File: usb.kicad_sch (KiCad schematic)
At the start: 134 parts, among them J3 USB4105-GF-A, J4 WE_632723300011_alt_symbol, Q1 NX138BKMYL, Q2 NX138BKMYL, Q3 NX138BKMYL, U10 TUSB1046-DCI, U11 TPD4E05U06QDQARQ1, U12 AP22615, U13 TPD4E05U06QDQARQ1, U14 TPD4E05U06QDQARQ1, U15 TPD4E05U06QDQARQ1, U16 TPD4E05U06QDQARQ1, U5 FT230XQ-R, U6 TPS65988, U7 W25Q80DVUXIE_TR, U8 TPS7B8133DRVR, U9 AP22615

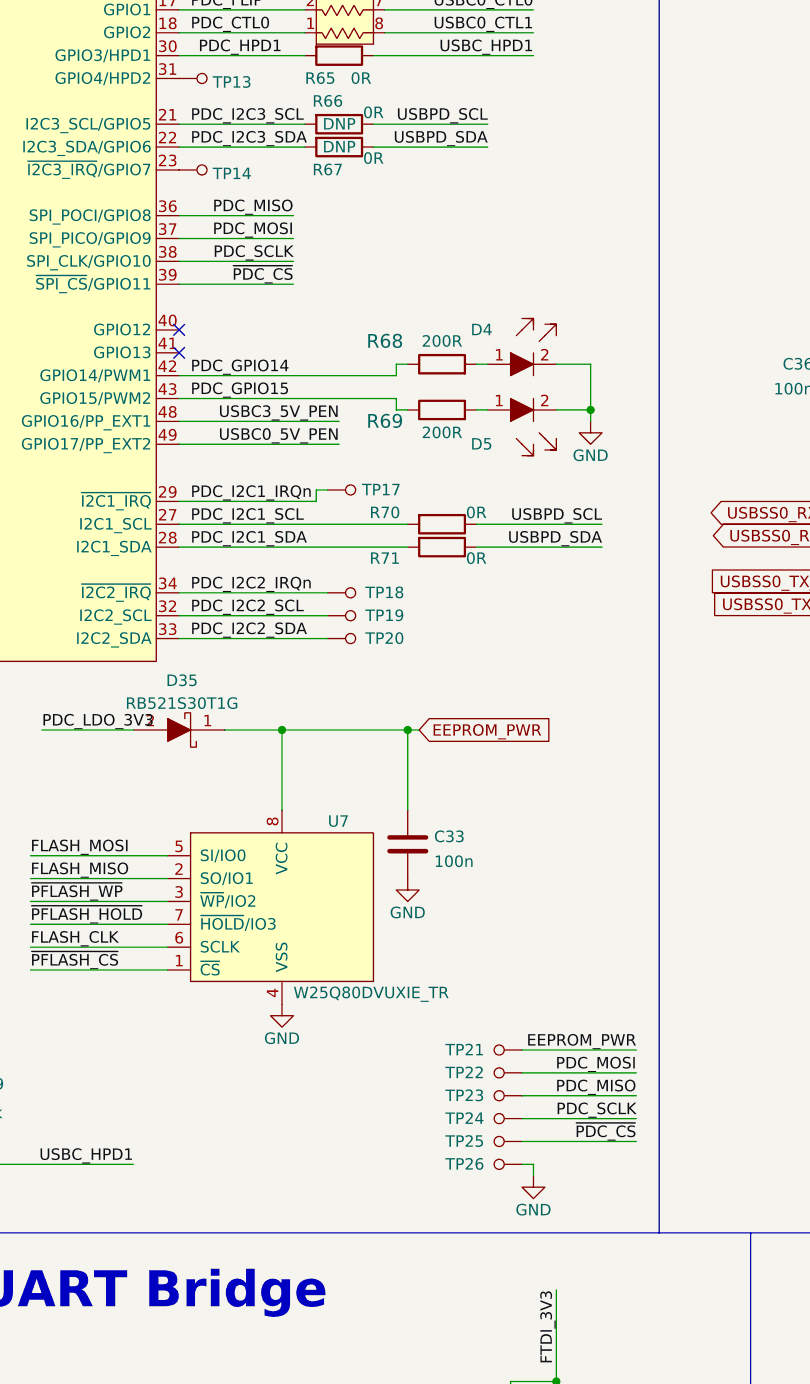
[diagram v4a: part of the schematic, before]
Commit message: Routed more low speed signal and power
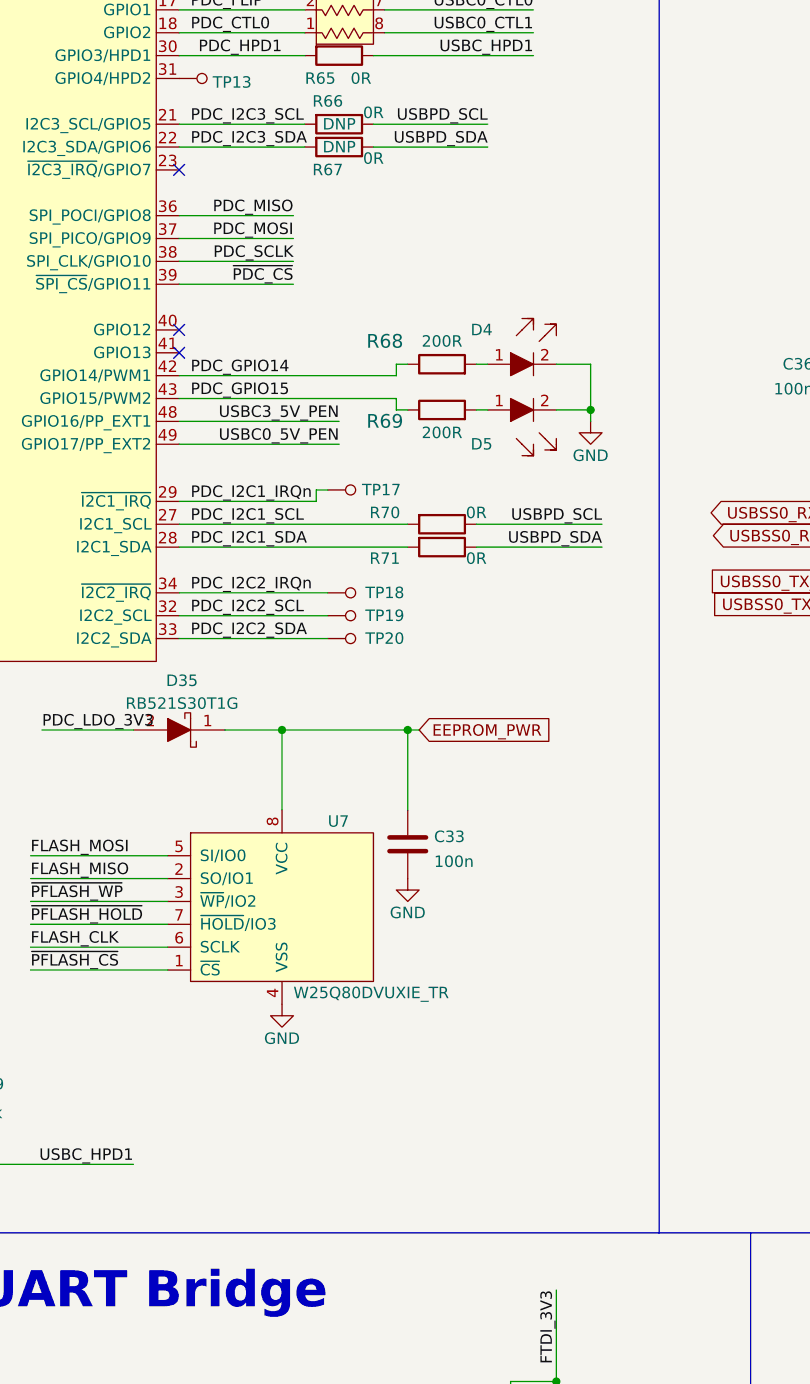
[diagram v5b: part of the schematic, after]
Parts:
- removed TP14, TP21, TP22, TP23, TP24, TP25, TP26: TP_SMD_0_75MM, antmicro-footprints:Testpoint_smd_0_75mm, symbol antmicroTestPoints:TP_SMD_0_75MM
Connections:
- no-connect marks 17 -> 18
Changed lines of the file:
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@@
   (no_connect (at 265.43 262.89))
   (no_connect (at 90.17 215.9))
+  (no_connect (at 92.71 63.5))
   (no_connect (at 292.1 135.89))
   (no_connect (at 294.64 135.89))
@@
     (stroke (width 0) (type solid) (color 0 0 0 0))
   )
-  (wire (pts (xy 143.51 168.91) (xy 130.81 168.91))
-    (stroke (width 0) (type default) (color 0 0 0 0))
-  )
   (wire (pts (xy 255.27 63.5) (xy 255.27 64.77))
     (stroke (width 0) (type default) (color 0 0 0 0))
@@
     (stroke (width 0) (type default) (color 0 0 0 0))
   )
-  (wire (pts (xy 130.81 173.99) (xy 132.08 173.99))
-    (stroke (width 0) (type default) (color 0 0 0 0))
-  )
   (wire (pts (xy 261.62 48.26) (xy 275.59 48.26))
     (stroke (width 0) (type default) (color 0 0 0 0))
@@
     (stroke (width 0) (type default) (color 0 0 0 0))
   )
-  (wire (pts (xy 143.51 171.45) (xy 130.81 171.45))
-    (stroke (width 0) (type default) (color 0 0 0 0))
-  )
   (wire (pts (xy 220.98 218.44) (xy 220.98 219.71))
     (stroke (width 0) (type default) (color 0 0 0 0))
@@
     (stroke (width 0) (type default) (color 0 0 0 0))
   )
-  (wire (pts (xy 132.08 173.99) (xy 132.08 175.26))
-    (stroke (width 0) (type default) (color 0 0 0 0))
-  )
   (wire (pts (xy 295.91 58.42) (xy 295.91 59.69))
     (stroke (width 0) (type default) (color 0 0 0 0))
@@
     (stroke (width 0) (type solid) (color 0 0 0 0))
   )
-  (wire (pts (xy 143.51 163.83) (xy 130.81 163.83))
-    (stroke (width 0) (type default) (color 0 0 0 0))
-  )
   (wire (pts (xy 361.95 64.77) (xy 361.95 78.74))
     (stroke (width 0) (type default) (color 0 0 0 0))
@@
     (stroke (width 0) (type default) (color 0 0 0 0))
   )
-  (wire (pts (xy 130.81 161.29) (xy 143.51 161.29))
-    (stroke (width 0) (type default) (color 0 0 0 0))
-  )
   (wire (pts (xy 238.76 255.27) (xy 245.11 255.27))
     (stroke (width 0) (type default) (color 0 0 0 0))
@@
     (stroke (width 0) (type default) (color 0 0 0 0))
   )
-  (wire (pts (xy 143.51 166.37) (xy 130.81 166.37))
-    (stroke (width 0) (type default) (color 0 0 0 0))
-  )
   (wire (pts (xy 236.22 124.46) (xy 273.05 124.46))
     (stroke (width 0) (type default) (color 0 0 0 0))
@@
     (effects (font (size 1.27 1.27)) (justify left bottom))
   )
-  (label "PDC_MOSI" (at 143.51 163.83 180)
-    (effects (font (size 1.27 1.27)) (justify right bottom))
-  )
   (label "USBC0_RX1_P" (at 238.76 101.6 0)
     (effects (font (size 1.27 1.27)) (justify left bottom))
@@
     (effects (font (size 1.27 1.27)) (justify left bottom))
   )
-  (label "~{PDC_CS}" (at 143.51 171.45 180)
-    (effects (font (size 1.27 1.27)) (justify right bottom))
-  )
   (label "USBC0_EQ1" (at 237.49 162.56 0)
     (effects (font (size 1.27 1.27)) (justify left bottom))
@@
     (effects (font (size 1.27 1.27)) (justify left bottom))
   )
-  (label "PDC_SCLK" (at 143.51 168.91 180)
-    (effects (font (size 1.27 1.27)) (justify right bottom))
-  )
   (label "FLASH_MOSI" (at 76.2 139.7 0)
     (effects (font (size 1.27 1.27)) (justify left bottom))
@@
     (effects (font (size 1.27 1.27)) (justify left bottom))
   )
-  (label "EEPROM_PWR" (at 143.51 161.29 180)
-    (effects (font (size 1.27 1.27)) (justify right bottom))
-  )
   (label "FTDI_LED_RX" (at 148.59 219.71 180)
     (effects (font (size 1.27 1.27)) (justify right bottom))
@@
     (effects (font (size 1.27 1.27)) (justify left bottom))
   )
-  (label "PDC_MISO" (at 143.51 166.37 180)
-    (effects (font (size 1.27 1.27)) (justify right bottom))
-  )
   (label "FTDI_LED_RX" (at 93.98 222.25 180)
     (effects (font (size 1.27 1.27)) (justify right bottom))
@@
     (pin "1")
   )
-  (symbol (lib_id "antmicroTestPoints:TP_SMD_0_75MM") (at 128.27 171.45 270) (unit 1)
-    (in_bom yes) (on_board yes)
-    (property "Reference" "TP25" (id 0) (at 124.46 171.45 90))
-    (property "Value" "TP_SMD_0_75MM" (id 1) (at 125.73 171.45 0)
-      (effects (font (size 1.27 1.27)) hide)
-    )
-    (property "Footprint" "antmicro-footprints:Testpoint_smd_0_75mm" (id 2) (at 133.35 176.53 0)
-      (effects (font (size 1.524 1.524)) (justify left) hide)
-    )
-    (property "Datasheet" "" (id 3) (at 135.89 176.53 0)
-      (effects (font (size 1.524 1.524)) (justify left) hide)
-    )
-    (pin "1")
-  )
   (symbol (lib_id "antmicroTVSDiodes:TPD4E05U06QDQARQ1") (at 318.77 137.16 270) (unit 1)
     (in_bom yes) (on_board yes) (fields_autoplaced)
@@
     (pin "3")
   )
-  (symbol (lib_id "antmicroTestPoints:TP_SMD_0_75MM") (at 128.27 168.91 270) (unit 1)
-    (in_bom yes) (on_board yes)
-    (property "Reference" "TP24" (id 0) (at 124.46 168.91 90))
-    (property "Value" "TP_SMD_0_75MM" (id 1) (at 125.73 168.91 0)
-      (effects (font (size 1.27 1.27)) hide)
-    )
-    (property "Footprint" "antmicro-footprints:Testpoint_smd_0_75mm" (id 2) (at 133.35 173.99 0)
-      (effects (font (size 1.524 1.524)) (justify left) hide)
-    )
-    (property "Datasheet" "" (id 3) (at 135.89 173.99 0)
-      (effects (font (size 1.524 1.524)) (justify left) hide)
-    )
-    (pin "1")
-  )
   (symbol (lib_id "antmicroResistors0402:R_0R_0402") (at 242.57 74.93 90) (unit 1)
     (in_bom no) (on_board yes)
@@
     (pin "2")
   )
-  (symbol (lib_id "antmicroTestPoints:TP_SMD_0_75MM") (at 128.27 166.37 270) (unit 1)
-    (in_bom yes) (on_board yes)
-    (property "Reference" "TP23" (id 0) (at 124.46 166.37 90))
-    (property "Value" "TP_SMD_0_75MM" (id 1) (at 125.73 166.37 0)
-      (effects (font (size 1.27 1.27)) hide)
-    )
-    (property "Footprint" "antmicro-footprints:Testpoint_smd_0_75mm" (id 2) (at 133.35 171.45 0)
-      (effects (font (size 1.524 1.524)) (justify left) hide)
-    )
-    (property "Datasheet" "" (id 3) (at 135.89 171.45 0)
-      (effects (font (size 1.524 1.524)) (justify left) hide)
-    )
-    (pin "1")
-  )
   (symbol (lib_id "antmicroPMICVoltageRegulatorsLinear:TPS7B8133DRVR") (at 121.92 256.54 0) (unit 1)
     (in_bom yes) (on_board yes) (fields_autoplaced)
@@
     (pin "1")
   )
-  (symbol (lib_id "antmicroTestPoints:TP_SMD_0_75MM") (at 128.27 161.29 270) (unit 1)
-    (in_bom yes) (on_board yes)
-    (property "Reference" "TP21" (id 0) (at 124.46 161.29 90))
-    (property "Value" "TP_SMD_0_75MM" (id 1) (at 125.73 161.29 0)
-      (effects (font (size 1.27 1.27)) hide)
-    )
-    (property "Footprint" "antmicro-footprints:Testpoint_smd_0_75mm" (id 2) (at 133.35 166.37 0)
-      (effects (font (size 1.524 1.524)) (justify left) hide)
-    )
-    (property "Datasheet" "" (id 3) (at 135.89 166.37 0)
-      (effects (font (size 1.524 1.524)) (justify left) hide)
-    )
-    (pin "1")
-  )
   (symbol (lib_id "antmicroResistors0402:R_1k_0402") (at 269.24 167.64 0) (unit 1)
     (in_bom yes) (on_board yes)
@@
     (pin "2")
   )
-  (symbol (lib_id "antmicroTestPoints:TP_SMD_0_75MM") (at 128.27 173.99 270) (unit 1)
-    (in_bom yes) (on_board yes)
-    (property "Reference" "TP26" (id 0) (at 124.46 173.99 90))
-    (property "Value" "TP_SMD_0_75MM" (id 1) (at 125.73 173.99 0)
-      (effects (font (size 1.27 1.27)) hide)
-    )
-    (property "Footprint" "antmicro-footprints:Testpoint_smd_0_75mm" (id 2) (at 133.35 179.07 0)
-      (effects (font (size 1.524 1.524)) (justify left) hide)
-    )
-    (property "Datasheet" "" (id 3) (at 135.89 179.07 0)
-      (effects (font (size 1.524 1.524)) (justify left) hide)
-    )
-    (pin "1")
-  )
   (symbol (lib_id "antmicroTransistorsFETsMOSFETsSingle:NX138BKMYL") (at 58.42 173.99 270) (unit 1)
     (in_bom yes) (on_board yes)
@@
     (pin "2")
   )
-  (symbol (lib_id "antmicroTestPoints:TP_SMD_0_75MM") (at 128.27 163.83 270) (unit 1)
-    (in_bom yes) (on_board yes)
-    (property "Reference" "TP22" (id 0) (at 124.46 163.83 90))
-    (property "Value" "TP_SMD_0_75MM" (id 1) (at 125.73 163.83 0)
-      (effects (font (size 1.27 1.27)) hide)
-    )
-    (property "Footprint" "antmicro-footprints:Testpoint_smd_0_75mm" (id 2) (at 133.35 168.91 0)
-      (effects (font (size 1.524 1.524)) (justify left) hide)
-    )
-    (property "Datasheet" "" (id 3) (at 135.89 168.91 0)
-      (effects (font (size 1.524 1.524)) (justify left) hide)
-    )
-    (pin "1")
-  )
   (symbol (lib_id "power:GND") (at 332.74 137.16 0) (unit 1)
     (in_bom yes) (on_board yes) (fields_autoplaced)
@@
     (pin "2")
   )
-  (symbol (lib_id "antmicroTestPoints:TP_SMD_0_75MM") (at 95.25 63.5 90) (unit 1)
-    (in_bom yes) (on_board yes) (fields_autoplaced)
-    (property "Reference" "TP14" (id 0) (at 96.4438 63.9338 90)
-      (effects (font (size 1.27 1.27)) (justify right))
-    )
-    (property "Value" "TP_SMD_0_75MM" (id 1) (at 97.79 63.5 0)
-      (effects (font (size 1.27 1.27)) hide)
-    )
-    (property "Footprint" "antmicro-footprints:Testpoint_smd_0_75mm" (id 2) (at 90.17 58.42 0)
-      (effects (font (size 1.524 1.524)) (justify left) hide)
-    )
-    (property "Datasheet" "" (id 3) (at 87.63 58.42 0)
-      (effects (font (size 1.524 1.524)) (justify left) hide)
-    )
-    (pin "1")
-  )
   (symbol (lib_id "antmicroLEDIndicationDiscrete:LTST-C190GKT") (at 132.08 90.17 0) (mirror x) (unit 1)
     (in_bom yes) (on_board yes)
@@
     (pin "Shell")
   )
-  (symbol (lib_id "power:GND") (at 132.08 175.26 0) (unit 1)
-    (in_bom yes) (on_board yes)
-    (property "Reference" "#PWR064" (id 0) (at 132.08 181.61 0)
-      (effects (font (size 1.27 1.27)) hide)
-    )
-    (property "Value" "GND" (id 1) (at 132.08 179.07 0))
-    (property "Footprint" "" (id 2) (at 132.08 175.26 0)
-      (effects (font (size 1.27 1.27)) hide)
-    )
-    (property "Datasheet" "" (id 3) (at 132.08 175.26 0)
-      (effects (font (size 1.27 1.27)) hide)
-    )
-    (pin "1")
-  )
   (symbol (lib_id "antmicroResistors0402:R_2k2_0402") (at 220.98 213.36 90) (unit 1)

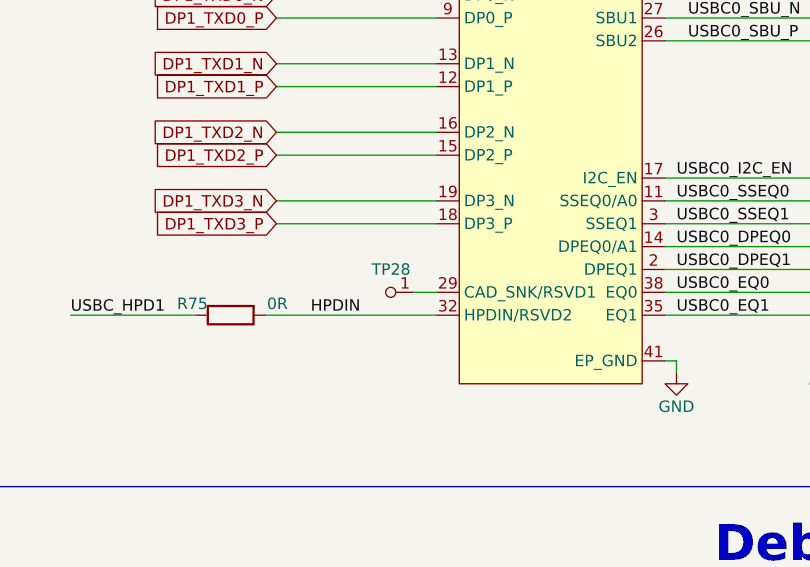
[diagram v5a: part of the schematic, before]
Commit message: Fixed DRC errors, fixed swapped SDA/SCL
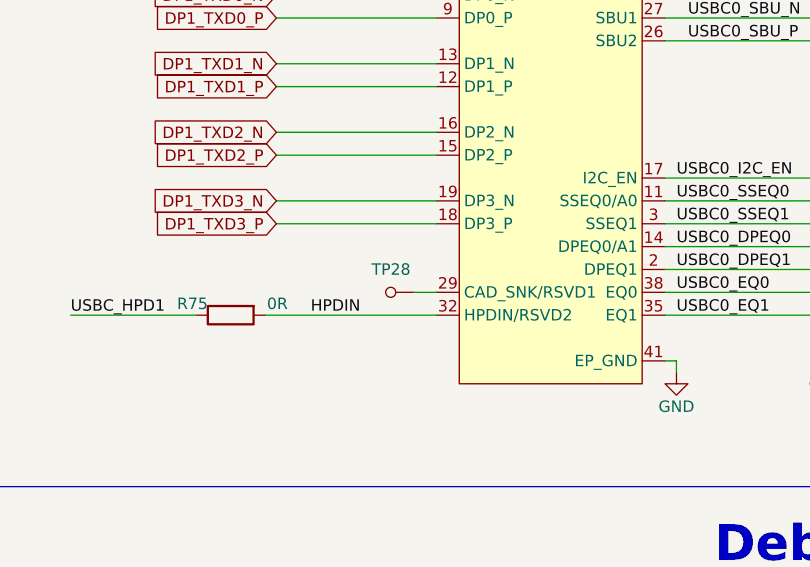
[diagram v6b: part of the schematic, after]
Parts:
- TP28: footprint antmicro-footprints:TP-R-1.5 -> antmicro-footprints:Testpoint_smd_0_75mm; symbol antmicroTestPoints:TP -> antmicroTestPoints:TP_SMD_0_75MM
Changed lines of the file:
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@@
     (pin "2")
   )
-  (symbol (lib_id "antmicroTestPoints:TP") (at 205.74 160.02 270) (unit 1)
+  (symbol (lib_id "antmicroTestPoints:TP_SMD_0_75MM") (at 205.74 160.02 270) (unit 1)
     (in_bom yes) (on_board yes) (fields_autoplaced)
     (property "Reference" "TP28" (id 0) (at 205.7781 157.48 90))
@@
       (effects (font (size 1.27 1.27)) hide)
     )
-    (property "Footprint" "antmicro-footprints:TP-R-1.5" (id 2) (at 205.74 160.02 0)
-      (effects (font (size 1.27 1.27)) hide)
+    (property "Footprint" "antmicro-footprints:Testpoint_smd_0_75mm" (id 2) (at 210.82 165.1 0)
+      (effects (font (size 1.524 1.524)) (justify left) hide)
     )
-    (property "Datasheet" "" (id 3) (at 205.74 160.02 0)
-      (effects (font (size 1.27 1.27)) hide)
+    (property "Datasheet" "" (id 3) (at 213.36 165.1 0)
+      (effects (font (size 1.524 1.524)) (justify left) hide)
     )
     (pin "1")

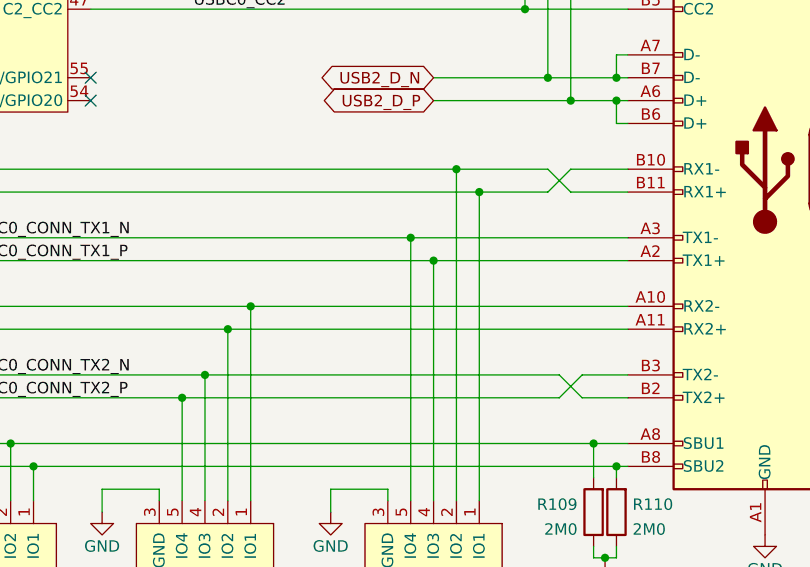
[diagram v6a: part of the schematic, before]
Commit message: Fixed swapped CSI signals
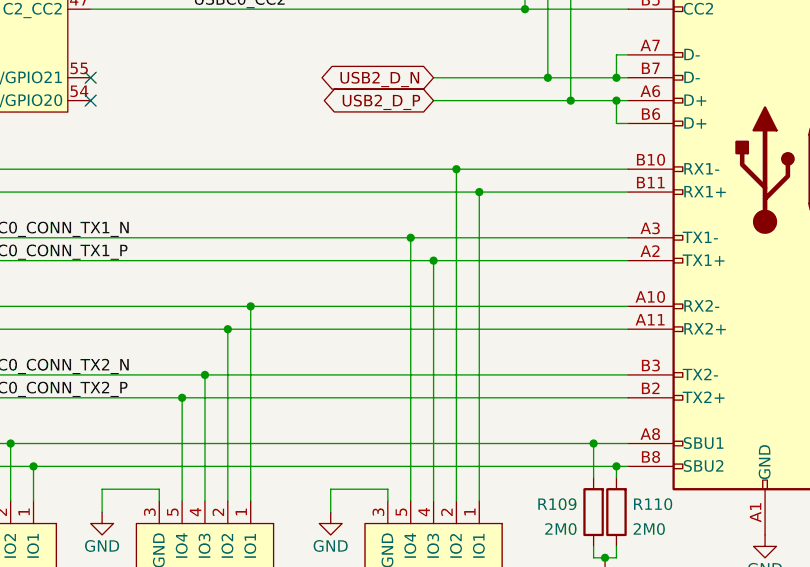
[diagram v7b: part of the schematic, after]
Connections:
- net USBC0_CONN_TX2_N: now also J4.B3 (TX2-); no longer J4.B2 (TX2+)
- net USBC0_CONN_TX2_P: now also J4.B2 (TX2+); no longer J4.B3 (TX2-)
- net USBC0_RX1_N: now also J4.B10 (RX1-); no longer J4.B11 (RX1+)
- net USBC0_RX1_P: now also J4.B11 (RX1+); no longer J4.B10 (RX1-)
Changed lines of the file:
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@@
-    (stroke (width 0) (type default) (color 0 0 0 0))
-  )
-  (wire (pts (xy 358.14 121.92) (xy 360.68 124.46))
     (stroke (width 0) (type default) (color 0 0 0 0))
   )
@@
     (stroke (width 0) (type default) (color 0 0 0 0))
   )
-  (wire (pts (xy 356.87 99.06) (xy 359.41 101.6))
-    (stroke (width 0) (type default) (color 0 0 0 0))
-  )
   (wire (pts (xy 171.45 101.6) (xy 168.91 104.14))
     (stroke (width 0) (type default) (color 0 0 0 0))
@@
   )
   (wire (pts (xy 242.57 83.82) (xy 259.08 83.82))
-    (stroke (width 0) (type default) (color 0 0 0 0))
-  )
-  (wire (pts (xy 359.41 99.06) (xy 365.76 99.06))
     (stroke (width 0) (type default) (color 0 0 0 0))
   )
@@
     (stroke (width 0) (type default) (color 0 0 0 0))
   )
-  (wire (pts (xy 360.68 121.92) (xy 365.76 121.92))
+  (wire (pts (xy 318.77 121.92) (xy 365.76 121.92))
     (stroke (width 0) (type default) (color 0 0 0 0))
   )
@@
     (stroke (width 0) (type default) (color 0 0 0 0))
   )
-  (wire (pts (xy 359.41 101.6) (xy 365.76 101.6))
-    (stroke (width 0) (type default) (color 0 0 0 0))
-  )
   (wire (pts (xy 344.17 91.44) (xy 359.41 91.44))
     (stroke (width 0) (type default) (color 0 0 0 0))
@@
     (stroke (width 0) (type default) (color 0 0 0 0))
   )
-  (wire (pts (xy 316.23 124.46) (xy 358.14 124.46))
-    (stroke (width 0) (type default) (color 0 0 0 0))
-  )
   (wire (pts (xy 273.05 139.7) (xy 276.86 139.7))
     (stroke (width 0) (type default) (color 0 0 0 0))
@@
     (stroke (width 0) (type default) (color 0 0 0 0))
   )
-  (wire (pts (xy 359.41 99.06) (xy 356.87 101.6))
-    (stroke (width 0) (type default) (color 0 0 0 0))
-  )
   (wire (pts (xy 344.17 109.22) (xy 365.76 109.22))
     (stroke (width 0) (type default) (color 0 0 0 0))
@@
     (stroke (width 0) (type default) (color 0 0 0 0))
   )
-  (wire (pts (xy 349.25 101.6) (xy 356.87 101.6))
+  (wire (pts (xy 349.25 101.6) (xy 365.76 101.6))
     (stroke (width 0) (type default) (color 0 0 0 0))
   )
@@
     (stroke (width 0) (type default) (color 0 0 0 0))
   )
-  (wire (pts (xy 346.71 99.06) (xy 356.87 99.06))
+  (wire (pts (xy 346.71 99.06) (xy 365.76 99.06))
     (stroke (width 0) (type default) (color 0 0 0 0))
   )
@@
     (stroke (width 0) (type default) (color 0 0 0 0))
   )
-  (wire (pts (xy 318.77 121.92) (xy 358.14 121.92))
-    (stroke (width 0) (type default) (color 0 0 0 0))
-  )
   (wire (pts (xy 92.71 68.58) (xy 105.41 68.58))
     (stroke (width 0) (type default) (color 0 0 0 0))
@@
     (stroke (width 0) (type default) (color 0 0 0 0))
   )
-  (wire (pts (xy 360.68 124.46) (xy 365.76 124.46))
+  (wire (pts (xy 316.23 124.46) (xy 365.76 124.46))
     (stroke (width 0) (type default) (color 0 0 0 0))
   )
@@
     (stroke (width 0) (type default) (color 0 0 0 0))
   )
-  (wire (pts (xy 360.68 121.92) (xy 358.14 124.46))
-    (stroke (width 0) (type default) (color 0 0 0 0))
-  )
